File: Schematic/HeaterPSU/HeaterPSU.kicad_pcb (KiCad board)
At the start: 2 copper layers, 100 x 35 mm, 56 parts, among them J201 To MCU Board, J202 SMPS2_SEC, J203 Heater Output, Q201 IRF4905, Q202 BC847, Q203 BC847, Q204 BC857, Q205 IRF4905, SW201 SW_Rotary_1P5T_ALPSALPINE_SRBV, U201 L78L12_SOT89, U202 TPS54302

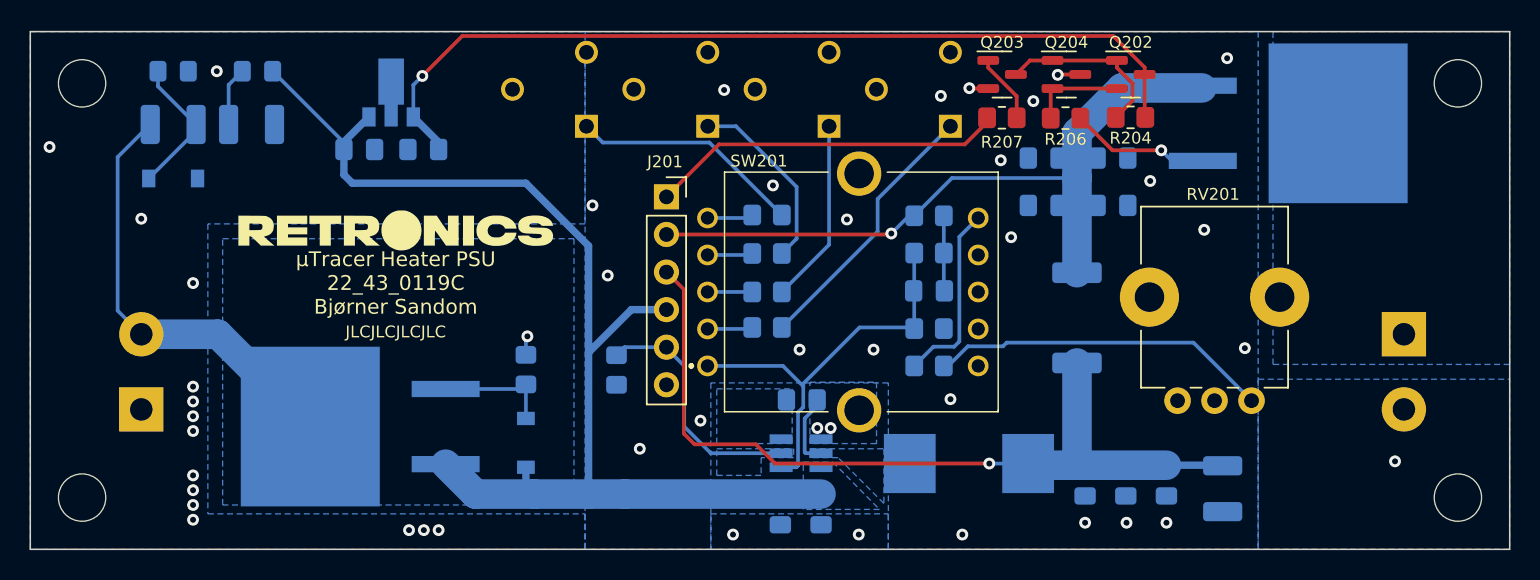
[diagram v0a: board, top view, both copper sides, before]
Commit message: New PSU based on XL4005
Added current limiter
Added interface to uTracer PIC
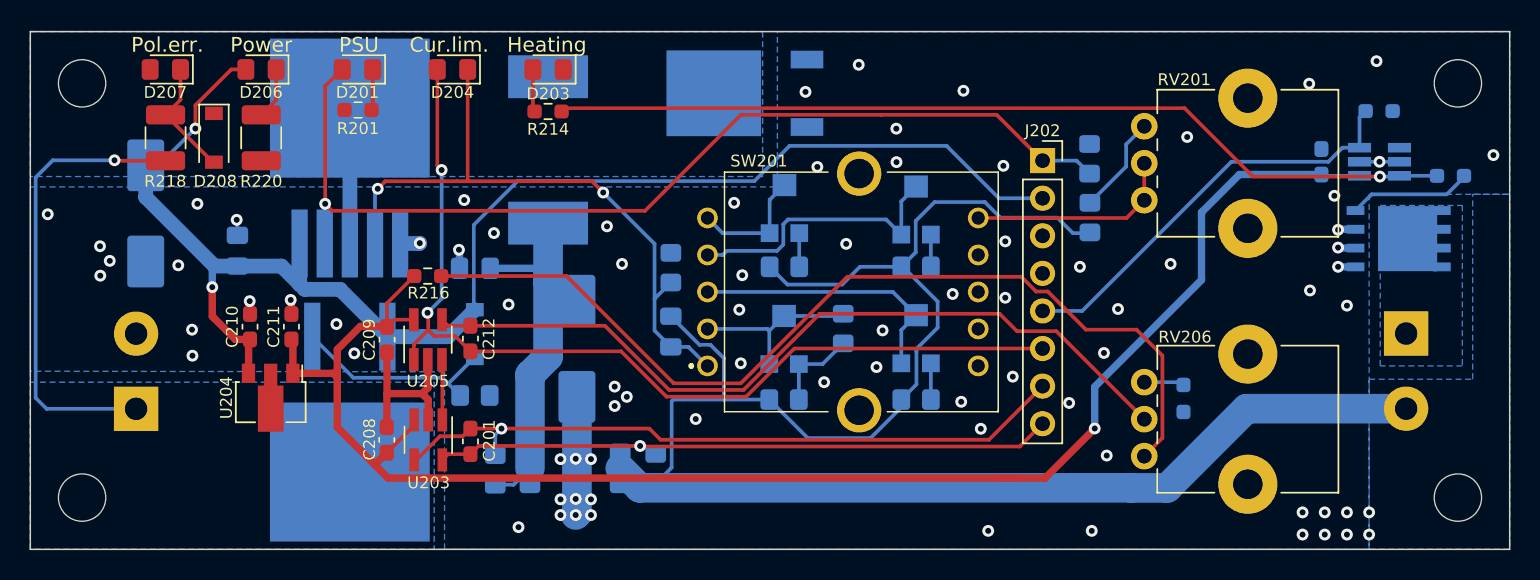
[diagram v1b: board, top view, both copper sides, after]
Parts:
- removed the C210 at (123.5, 53.5)
- removed the C211 at (105.7, 77.3)
- removed C213: 75pF, Capacitor_SMD:C_0805_2012Metric_Pad1.18x1.45mm_HandSolder
- removed the Q202 at (129.4, 47.9)
- removed Q203: BC847, Package_TO_SOT_SMD:SOT-23
- removed Q204: BC857, Package_TO_SOT_SMD:SOT-23
- removed Q205: IRF4905, Package_TO_SOT_SMD:TO-263-2
- removed the R204 at (129.4, 50.8)
- removed the R218 at (104.8, 65.0)
- added C201: 1µF, Capacitor_SMD:C_0603_1608Metric_Pad1.08x0.95mm_HandSolder, F.Cu at (84.8, 72.7)
- added C202: 470µF 35V, Capacitor_SMD:CP_Elec_8x10, B.Cu at (62.8, 57.3)
- added D201: "PSU On", LED_SMD:LED_0805_2012Metric_Pad1.15x1.40mm_HandSolder, F.Cu at (77.1, 47.6)
- added D202: VS-50WQ04FN, Package_TO_SOT_SMD:TO-252-2, B.Cu at (103.3, 49.2)
- added D203: "Out en", LED_SMD:LED_0805_2012Metric_Pad1.15x1.40mm_HandSolder, F.Cu at (90.0, 47.6)
- added D204: "Current limiter", LED_SMD:LED_0805_2012Metric_Pad1.15x1.40mm_HandSolder, F.Cu at (83.5, 47.6)
- added Q201: SIRA24DP-T1-GE3, myDevices:SIRA24DP-T1-GE3, B.Cu at (147.5, 59.0)
- added R201: 560Ω, Resistor_SMD:R_0603_1608Metric_Pad0.98x0.95mm_HandSolder, F.Cu at (77.2, 50.3)
- added R202: 10Ω, Resistor_SMD:R_0805_2012Metric_Pad1.20x1.40mm_HandSolder, B.Cu at (86.4, 74.6)
- added R203: 10Ω, Resistor_SMD:R_0805_2012Metric_Pad1.20x1.40mm_HandSolder, B.Cu at (97.3, 74.5)
- added R205: 300Ω, Resistor_SMD:R_0805_2012Metric_Pad1.20x1.40mm_HandSolder, B.Cu at (126.6, 57.6)
- added R208: 1.3kΩ, Resistor_SMD:R_0805_2012Metric_Pad1.20x1.40mm_HandSolder, B.Cu at (114.9, 69.9)
- added RV206: 10kΩ, Potentiometer_THT:Potentiometer_Bourns_PTV09A-1_Single_Vertical, F.Cu at (130.3, 73.7)
- added U203: INA293B, Package_TO_SOT_SMD:SOT-23-5_HandSoldering, F.Cu at (81.9, 72.6)
- added U204: L78L05_SOT89, Package_TO_SOT_SMD:SOT-89-3, F.Cu at (71.2, 69.8)
- added U205: TS321, Package_TO_SOT_SMD:SOT-23-5_HandSoldering, F.Cu at (81.9, 65.8)
- C203: value 100nF -> 1µF 50V
- C204: value 22µF 25V -> 1µF 50V
- C205: value 22µF 25V -> 470µF 35V; footprint Capacitor_SMD:C_0805_2012Metric_Pad1.18x1.45mm_HandSolder -> Capacitor_SMD:CP_Elec_8x10
- C206: value 22µF 25V -> 100nF; footprint Capacitor_SMD:C_0805_2012Metric_Pad1.18x1.45mm_HandSolder -> Capacitor_SMD:C_0603_1608Metric_Pad1.08x0.95mm_HandSolder
- C207: value 22µF 25V -> 10nF
- C208, C209: value 22µF 25V -> 100nF; footprint Capacitor_SMD:C_0805_2012Metric_Pad1.18x1.45mm_HandSolder -> Capacitor_SMD:C_0603_1608Metric_Pad1.08x0.95mm_HandSolder; moved to F.Cu
- C210: renamed from C201; footprint Capacitor_SMD:C_0805_2012Metric_Pad1.18x1.45mm_HandSolder -> Capacitor_SMD:C_0603_1608Metric_Pad1.08x0.95mm_HandSolder; moved to F.Cu
- C211: renamed from C202; value 100nF -> 1µF; footprint Capacitor_SMD:C_0805_2012Metric_Pad1.18x1.45mm_HandSolder -> Capacitor_SMD:C_0603_1608Metric_Pad1.08x0.95mm_HandSolder; moved to F.Cu
- C212: value 100nF -> 1µF; footprint Capacitor_SMD:C_0805_2012Metric_Pad1.18x1.45mm_HandSolder -> Capacitor_SMD:C_0603_1608Metric_Pad1.08x0.95mm_HandSolder; moved to F.Cu
- D206: renamed from D202; moved to F.Cu
- D207: renamed from D203; moved to F.Cu
- D208: renamed from D204; moved to F.Cu
- G***: moved to B.Cu
- J201: renamed from J202; value SMPS2_SEC -> Heater output
- J202: renamed from J201; footprint Connector_PinSocket_2.54mm:PinSocket_1x06_P2.54mm_Vertical -> Connector_PinSocket_2.54mm:PinSocket_1x08_P2.54mm_Vertical
- J203: value Heater Output -> SMPS2_SEC
- L201: value 22µH 4.1A -> 33µH 4.2A; footprint Inductor_SMD:L_Wuerth_HCI-1040 -> Inductor_SMD:L_12x12mm_H8mm
- R204: renamed from R208; value 25mΩ -> 10mΩ
- R206: value 47Ω -> 3.9kΩ; moved to B.Cu
- R207: value 1kΩ -> 1.8kΩ; moved to B.Cu
- R209: value 3.9kΩ 1/2W -> 180Ω; footprint Resistor_SMD:R_1210_3225Metric_Pad1.30x2.65mm_HandSolder -> Resistor_SMD:R_0805_2012Metric_Pad1.20x1.40mm_HandSolder
- R210: value 49.9Ω -> 10kΩ
- R211: value 100kΩ -> 270Ω
- R212: value 100kΩ -> 180Ω
- R213: value 470kΩ -> 47Ω; footprint Resistor_SMD:R_0805_2012Metric_Pad1.20x1.40mm_HandSolder -> Resistor_SMD:R_0603_1608Metric_Pad0.98x0.95mm_HandSolder
- R214: value 4.3kΩ -> 680Ω; footprint Resistor_SMD:R_0805_2012Metric_Pad1.20x1.40mm_HandSolder -> Resistor_SMD:R_0603_1608Metric_Pad0.98x0.95mm_HandSolder; moved to F.Cu
- R215: value 4.7kΩ -> 10kΩ; footprint Resistor_SMD:R_0805_2012Metric_Pad1.20x1.40mm_HandSolder -> Resistor_SMD:R_0603_1608Metric_Pad0.98x0.95mm_HandSolder
- R216: value 9.1kΩ -> 82kΩ; footprint Resistor_SMD:R_0805_2012Metric_Pad1.20x1.40mm_HandSolder -> Resistor_SMD:R_0603_1608Metric_Pad0.98x0.95mm_HandSolder; moved to F.Cu
- R217: value 13.3kΩ -> 1kΩ; footprint Resistor_SMD:R_0805_2012Metric_Pad1.20x1.40mm_HandSolder -> Resistor_SMD:R_0603_1608Metric_Pad0.98x0.95mm_HandSolder
- R218: renamed from R201; moved to F.Cu
- R220: renamed from R203; moved to F.Cu
- RV201: value 220kΩ -> 5kΩ
- RV202: value 1kΩ -> 200Ω; footprint Potentiometer_THT:Potentiometer_Runtron_RM-065_Vertical -> Potentiometer_SMD:Potentiometer_TT_35W
- RV203, RV204: value 2kΩ -> 200Ω; footprint Potentiometer_THT:Potentiometer_Runtron_RM-065_Vertical -> Potentiometer_SMD:Potentiometer_TT_35W
- RV205: value 50kΩ -> 200Ω; footprint Potentiometer_THT:Potentiometer_Runtron_RM-065_Vertical -> Potentiometer_SMD:Potentiometer_TT_35W
- SW201: value SW_Rotary_1P5T_ALPSALPINE_SRBV -> ALPSALPINE_SRBV_1P5T
- U201: value L78L12_SOT89 -> XL4005; footprint Package_TO_SOT_SMD:SOT-89-3 -> Package_TO_SOT_SMD:TO-263-5_TabPin3
- U202: value TPS54302 -> MCP14A0052T
- moved J203 85.8 mm to (62.1, 70.5), turned to 90 degrees
- moved J201 85.7 mm to (148.0, 65.4), turned to -90 degrees
- moved C208 51.5 mm to (79.1, 72.6), turned to -90 degrees
- moved C204 48.9 mm to (85.0, 61.0), turned to 180 degrees
- moved C209 45.3 mm to (79.1, 65.8), turned to 90 degrees
- moved U202 43.8 mm to (146.2, 53.8), turned to 0 degrees
- moved R215 42.0 mm to (146.2, 50.4), turned to 180 degrees
- moved C203 39.5 mm to (69.0, 59.8), turned to 90 degrees
- moved C205 38.2 mm to (92.0, 66.4), turned to -90 degrees
- moved R213 36.7 mm to (151.0, 54.8), turned to 180 degrees
- moved L201 35.5 mm to (90.0, 53.0), turned to -90 degrees
- moved R204 35.4 mm to (91.8, 74.5), turned to 0 degrees
- moved G*** 34.5 mm to (110.7, 73.6), turned to 180 degrees
- moved C207 32.1 mm to (98.3, 65.3), turned to 90 degrees
- moved R214 31.0 mm to (90.0, 50.4)
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- renumbered D201 to D205, Q201 to Q202, R202 to R219
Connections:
- C203 pad 1: Net-(C203-Pad1) -> VDC
- C203 pad 2: Net-(C203-Pad2) -> GNDPWR
- C204 pad 1: GNDPWR -> Net-(C204-Pad1)
- C204 pad 2: HeaterSense1 -> GNDPWR
- C205 pad 1: GNDPWR -> Net-(C204-Pad1)
- C205 pad 2: HeaterSense1 -> GNDPWR
- C206 pad 2: HeaterSense1 -> +5V
- C207 pad 1: GNDPWR -> Net-(C207-Pad1)
- C207 pad 2: HeaterSense2 -> Net-(C207-Pad2)
- C208 pad 2: HeaterSense2 -> +5V
- C209 pad 2: HeaterSense2 -> +5V
- C211 pad 2: Net-(Q202-Pad3) -> +5V
- C212 pad 1: GNDPWR -> CUR_LIM
- C212 pad 2: VDC -> Net-(C212-Pad2)
- J201 pad 1: GNDPWR -> Net-(J201-Pad1)
- J201 pad 2: Net-(J202-Pad2) -> Net-(C207-Pad2)
- J202 pad 1: Heater_PWM -> PSU_EN
- J202 pad 2: HeaterSense2 -> VDC
- J202 pad 3: HeaterSense1 -> GNDPWR
- J202 pad 4: VDC -> GNDPWR
- J202 pad 5: Heater_EN -> OUT_EN
- J202 pad 6: GNDPWR -> CUR_LIM
- J203 pad 1: /HeaterOutput -> Net-(J203-Pad1)
- L201 pad 1: Net-(C203-Pad1) -> Net-(D202-Pad2)
- L201 pad 2: HeaterSense1 -> Net-(C204-Pad1)
- Q202 pad 2: Net-(J202-Pad2) -> Net-(J203-Pad1)
- R204 pad 1: HeaterSense1 -> Net-(C204-Pad1)
- R204 pad 2: HeaterSense2 -> Net-(C207-Pad2)
- R206 pad 1: Net-(R206-Pad1) -> Net-(C207-Pad2)
- R206 pad 2: Net-(Q202-Pad2) -> Net-(R206-Pad2)
- R207 pad 1: Net-(Q203-Pad1) -> Net-(C207-Pad2)
- R207 pad 2: Heater_PWM -> Net-(R207-Pad2)
- R209 pad 1: HeaterSense1 -> Net-(C207-Pad2)
- R209 pad 2: GNDPWR -> Net-(R209-Pad2)
- R210 pad 1: HeaterSense2 -> GNDPWR
- R210 pad 2: Net-(C213-Pad2) -> PSU_EN
- R211 pad 1: Net-(C213-Pad2) -> Net-(C207-Pad1)
- R211 pad 2: /VSEL_COM -> GNDPWR
- R212 pad 1: GNDPWR -> Net-(R209-Pad2)
- R212 pad 2: Heater_EN -> /VSEL_1.4
- R213 pad 1: /VSEL_COM -> Net-(Q201-Pad2)
- R213 pad 2: GNDPWR -> Net-(R213-Pad2)
- R214 pad 1: /VSEL_VAR -> Net-(D203-Pad2)
- R214 pad 2: Net-(R214-Pad2) -> Net-(R213-Pad2)
- R215 pad 1: /VSEL_12.6 -> GNDPWR
- R215 pad 2: Net-(R215-Pad2) -> OUT_EN
- R216 pad 1: /VSEL_6.3 -> Net-(R216-Pad1)
- R216 pad 2: Net-(R216-Pad2) -> +5V
- R217 pad 1: /VSEL_5 -> GNDPWR
- R217 pad 2: Net-(R217-Pad2) -> Net-(RV206-Pad3)
- R218 pad 2: Net-(J202-Pad2) -> Net-(J203-Pad1)
- RV201 pad 1: Net-(R214-Pad2) -> /VSEL_VAR
- RV201 pad 2: GNDPWR -> /VSEL_VAR
- RV201 pad 3: GNDPWR -> Net-(R205-Pad2)
- RV202 pad 1: Net-(R215-Pad2) -> Net-(R206-Pad2)
- RV202 pad 2: GNDPWR -> /VSEL_12.6
- RV202 pad 3: GNDPWR -> /VSEL_12.6
- RV203 pad 1: Net-(R216-Pad2) -> Net-(R207-Pad2)
- RV203 pad 2: GNDPWR -> /VSEL_6.3
- RV203 pad 3: GNDPWR -> /VSEL_6.3
- RV204 pad 1: Net-(R217-Pad2) -> Net-(R208-Pad2)
- RV204 pad 2: GNDPWR -> /VSEL_5
- RV204 pad 3: GNDPWR -> /VSEL_5
- RV205 pad 1: Net-(R218-Pad2) -> Net-(R209-Pad2)
- RV205 pad 2: GNDPWR -> /VSEL_1.4
- RV205 pad 3: GNDPWR -> /VSEL_1.4
- SW201 pad 1: /VSEL_COM -> Net-(C207-Pad1)
- U201 pad 1: Net-(Q202-Pad3) -> GNDPWR
- U201 pad 2: GNDPWR -> Net-(C207-Pad1)
- U201 pad 3: VDC -> Net-(D202-Pad2)
- U202 pad 1: GNDPWR -> +5V
- U202 pad 2: Net-(C203-Pad1) -> GNDPWR
- U202 pad 3: VDC -> OUT_EN
- U202 pad 4: /VSEL_COM -> unconnected-(U202-Pad4)
- U202 pad 5: Heater_EN -> GNDPWR
- U202 pad 6: Net-(C203-Pad2) -> Net-(R213-Pad2)
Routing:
- net Net-(C207-Pad2): track 0.00 -> 128.0 mm
- net +5V: track 0.00 -> 108.3 mm, vias 0 -> 1
- net PSU_EN: track 0.00 -> 68.5 mm, vias 0 -> 1
- net CUR_LIM: track 0.00 -> 65.4 mm, vias 0 -> 2
- net Net-(R216-Pad1): track 0.00 -> 64.2 mm
- net Net-(R213-Pad2): track 0.00 -> 61.1 mm, vias 0 -> 1
- net Net-(Q202-Pad3): track 60.2 -> 0.00 mm, vias 1 -> 0
- net HeaterSense1: track 54.9 -> 0.00 mm, vias 1 -> 0
- net Net-(C212-Pad2): track 0.00 -> 54.5 mm
- net HeaterSense2: track 48.5 -> 0.00 mm, vias 1 -> 0
- net INA_VSENS: track 0.00 -> 47.1 mm, vias 0 -> 1
- net Net-(C207-Pad1): track 0.00 -> 44.1 mm, vias 0 -> 2
- net INA_CSENS: track 0.00 -> 41.6 mm, vias 0 -> 1
- net Net-(J203-Pad1): track 0.00 -> 31.3 mm, vias 0 -> 1
- net Net-(J202-Pad2): track 29.8 -> 0.00 mm
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- added copper zone on B.Cu, net Net-(D202-Pad2)
- added copper zone on B.Cu, net Net-(J201-Pad1)
- added copper zone on B.Cu, net Net-(J203-Pad1)
- removed copper zone on B.Cu, net /HeaterOutput
- removed copper zone on B.Cu, net Heater_EN
- removed copper zone on B.Cu, net Net-(C203-Pad1)
- removed copper zone on B.Cu, net Net-(C203-Pad2)
- removed copper zone on B.Cu, net Net-(J202-Pad2)
- removed copper zone on B.Cu, net VDC
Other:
- board text added: "+19V 0"
- board text added: "Cur.lim."
- board text added: "DC In"
- board text added: "H2 H1"
- board text added: "Heating"
- board text added: "PSU"
- board text added: "µTracer Heater PSU 22_43_0119D Bjørner Sandom"
- board text removed: "+ 0"
- board text removed: "."
- board text removed: "0 +19V"
- board text removed: "DC Input"
- board text removed: "µTracer Heater PSU 22_43_0119C Bjørner Sandom"

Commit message: Updated component values
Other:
- board text added: "."
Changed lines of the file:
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@@
     (effects (font (size 0.8 0.8) (thickness 0.15)) (justify mirror))
+  )
+  (gr_text "." (at 143.8 54.15) (layer "B.SilkS")
+    (effects (font (size 1.5 1.5) (thickness 0.3)) (justify mirror))
   )
   (gr_text "Heater out" (at 142.025 67.875 90) (layer "B.SilkS")

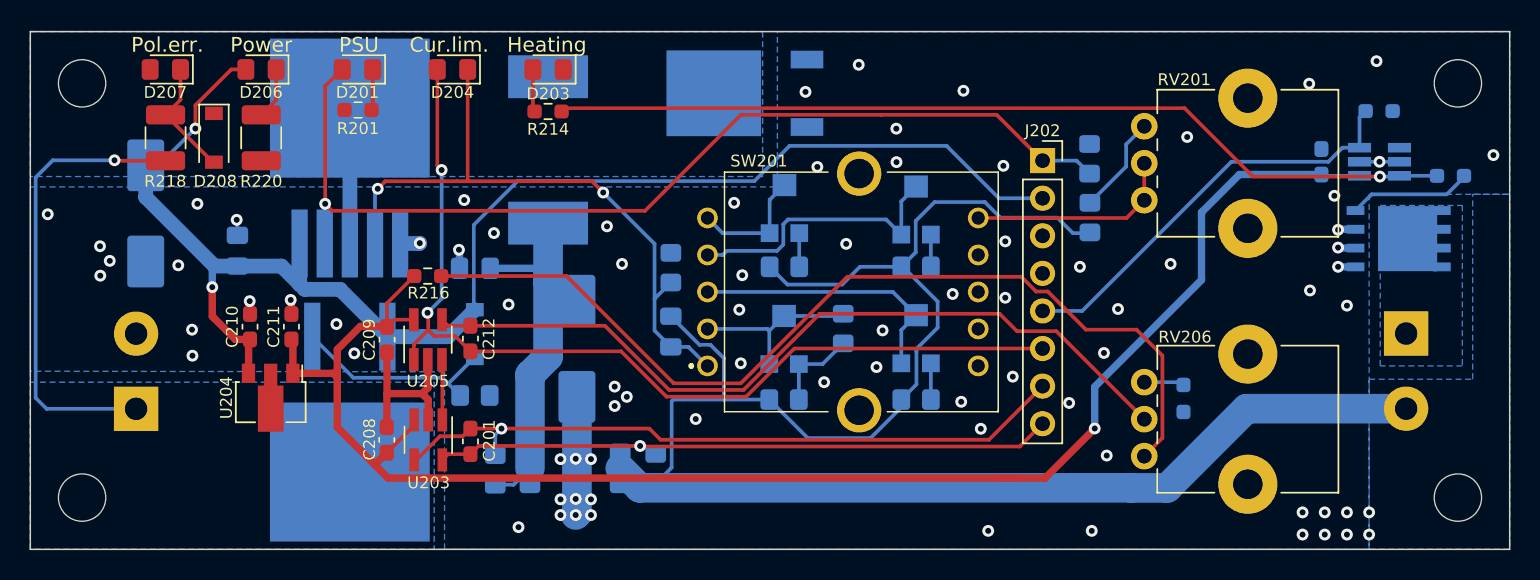
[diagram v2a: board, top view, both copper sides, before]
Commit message: Added output filter caps + spacing around mounting holes
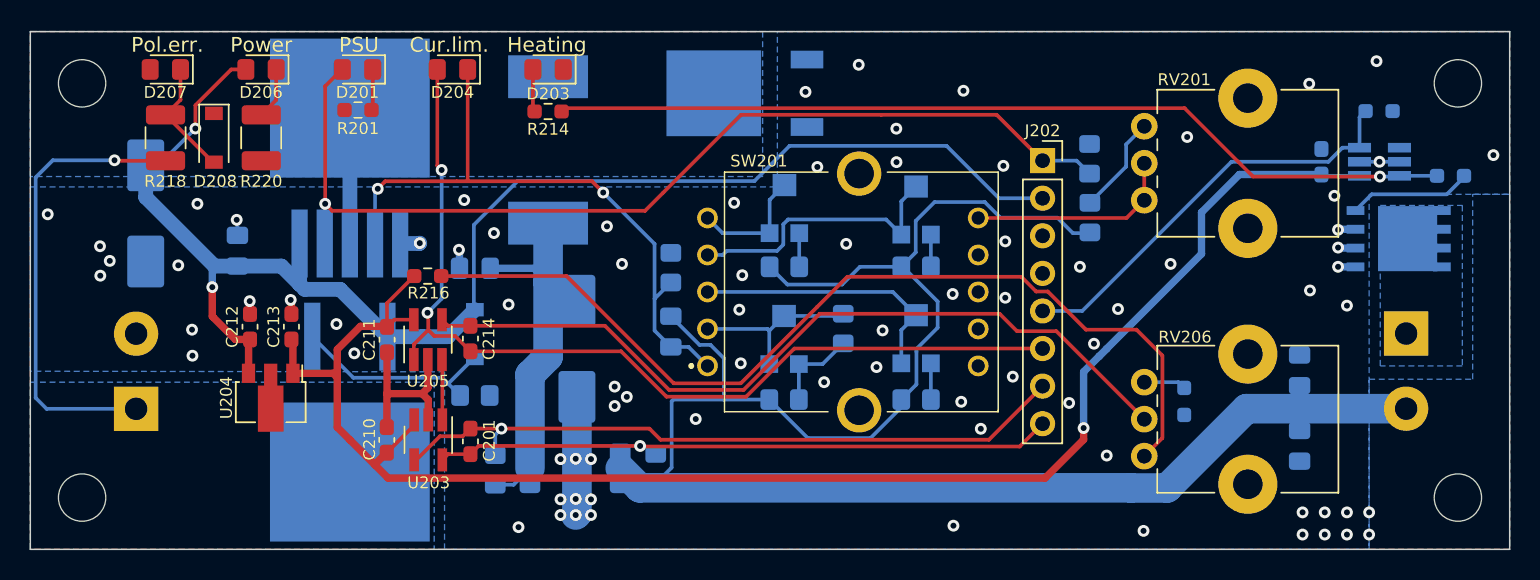
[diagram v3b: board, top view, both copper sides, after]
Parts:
- added C206: 22µF 25V, Capacitor_SMD:C_0805_2012Metric_Pad1.18x1.45mm_HandSolder, B.Cu at (140.8, 67.9)
- added C207: 22µF 25V, Capacitor_SMD:C_0805_2012Metric_Pad1.18x1.45mm_HandSolder, B.Cu at (140.8, 73.0)
- C212: renamed from C210; value 10µF 50V -> 10µF 35V
- Q201: value SIRA24DP-T1-GE3 -> SIRA24DP
- R205: value 300Ω -> 220Ω
- moved G*** 0.45 mm to (110.2, 73.6)
- moved R217 0.21 mm to (133.0, 70.0)
- renumbered C206 to C208, C207 to C209, C208 to C210, C209 to C211, C211 to C213, C212 to C214
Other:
- board text added: "H- H+"
- board text added: "µTracer Heater PSU 22_43_0119E Bjørner Sandom"
- board text removed: "H2 H1"
- board text removed: "µTracer Heater PSU 22_43_0119D Bjørner Sandom"

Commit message: Changed LED footprints to 0603
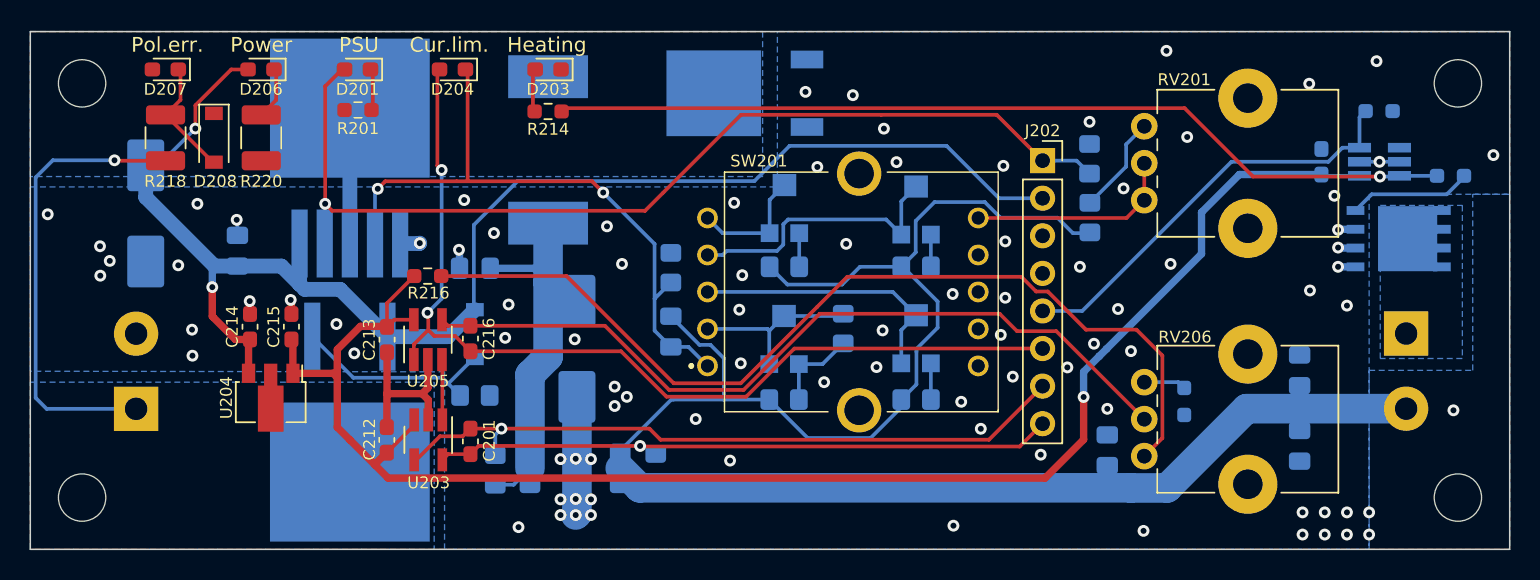
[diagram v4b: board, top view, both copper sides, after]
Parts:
- added C206: 22µF 25V, Capacitor_SMD:C_0805_2012Metric_Pad1.18x1.45mm_HandSolder, B.Cu at (127.8, 73.3)
- D201, D203, D204, D206, D207: footprint LED_SMD:LED_0805_2012Metric_Pad1.15x1.40mm_HandSolder -> LED_SMD:LED_0603_1608Metric_Pad1.05x0.95mm_HandSolder
- moved G*** 28.7 mm to (119.6, 46.5)
- renumbered C206 to C208, C207 to C209, C208 to C210, C209 to C211, C210 to C212, C211 to C213, C212 to C214, C213 to C215, C214 to C216
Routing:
- net GNDPWR: vias 82 -> 91
